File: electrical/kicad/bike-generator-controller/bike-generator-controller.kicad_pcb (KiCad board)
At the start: 2 copper layers, 100 x 115 mm, 60 parts, among them J1 DC_GEN_IN / DNP (DC VARIANT), J2 PHOENIX 1711725 / BUCK_IN, J3 J_DISPLAY_I2C, J5 J_EXT_GPIO, J6 LiPo 1S / JST-PH 2.0 / PROV., J7 J_CC_CTRL, J8 3PH_GEN_IN (1=U 2=V 3=W), J9 J_CV_CTRL, U1 INA228, U2 DFR0868 Beetle ESP32-C3, U3 MCP42100-I/SL, U4 LM5164DDAT

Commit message: wip: capture live PCB state before routing fixes
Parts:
- moved J8 8.42 mm to (61.5, 103.0)
- moved D2 7.93 mm to (71.9, 97.2)
- moved D1 3.42 mm to (84.2, 117.1)
- moved F1 3.11 mm to (79.5, 125.3)
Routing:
- net /INA228_SENSE/VBUS_SENSE: track 18.2 -> 50.1 mm
- net /POWER_PATH/RECTIFIED_RAW: track 0.00 -> 26.3 mm
- net Net-(D1-K): track 0.00 -> 11.5 mm
- net GND: track 34.9 -> 29.7 mm
- net /POWER_PATH/GEN_PHASE_V: track 12.7 -> 10.7 mm
- net /POWER_PATH/GEN_PHASE_W: track 13.7 -> 11.7 mm
- net /POWER_PATH/GEN_PHASE_U: track 12.5 -> 11.1 mm
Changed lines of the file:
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@@
 	(footprint "BikeGenerator:Fuse_Littelfuse_456_10.08x3.05mm_P9.35mm"
 		(layer "F.Cu")
-		(at 79.7375 128.4)
+		(at 79.525 125.3)
 		(descr "Littelfuse 456 Series High Current NANO2 fuse, 20A/25A/30A package. Exact recommended pad layout: pads 3.25 x 3.43 mm, 6.10 mm inner gap, 12.60 mm overall span, 9.35 mm center pitch. Body 10.08 x 3.05 mm. Pad numbering is arbitrary because the fuse is non-polarized: pad 1 left and pad 2 right in top/component view. Datasheet: https://www.littelfuse.com/assetdocs/littelfuse_fuse_456_datasheet.pdf?assetguid=d86b18f9-14fa-4764-87ff-8aec12e9a89d")
 		(property "Reference" "F1"
@@
 	(footprint "BikeGenerator:Diode_Bridge_Diotec_DBI-A_5Pin_P7.50mm"
 		(layer "F.Cu")
-		(at 73.8 104.9 -90)
+		(at 71.9 97.2 -90)
 		(descr "Diotec DBI25-xxA three-phase bridge rectifier, DBI-A vertical THT, five solder pins at 7.5 mm pitch; marking-side order left to right: - ~ ~ ~ +")
 		(property "Reference" "D2"
@@
 	(footprint "TerminalBlock_Phoenix:TerminalBlock_Phoenix_MKDS-3-3-5.08_1x03_P5.08mm_Horizontal"
 		(layer "F.Cu")
-		(at 61.7 111.4 90)
+		(at 61.4675 102.985 90)
 		(descr "Terminal Block Phoenix MKDS-3-3-5.08, 3 pins, pitch 5.08mm, size 15.2x11.2mm, drill diameter 1.3mm, pad diameter 2.6mm, http://www.farnell.com/datasheets/2138224.pdf")
 		(tags "THT Terminal Block Phoenix MKDS-3-3-5.08 pitch 5.08mm size 15.2x11.2mm drill 1.3mm pad 2.6mm")
@@
 	(footprint "Diode_SMD:D_SMC"
 		(layer "F.Cu")
-		(at 84.6 120.5 90)
+		(at 84.2 117.1 90)
 		(descr "Diode SMC (DO-214AB)")
 		(tags "Diode SMC (DO-214AB)")
@@
 	)
 	(segment
+		(start 84.2 113.7)
+		(end 83 112.5)
+		(width 2)
+		(layer "F.Cu")
+		(net "GND")
+	)
+	(segment
 		(start 91.7 87.9625)
 		(end 91.7 89.3)
@@
 	)
 	(segment
-		(start 83.5 116)
-		(end 83.5 114.5)
-		(width 2)
-		(layer "F.Cu")
-		(net "GND")
-	)
-	(segment
 		(start 91.075 114)
 		(end 91.075 111.5)
@@
 	)
 	(segment
+		(start 84.2 113.7)
+		(end 84.8 113.7)
+		(width 2)
+		(layer "F.Cu")
+		(net "GND")
+	)
+	(segment
 		(start 91.5 109.150001)
 		(end 91.5 111.4625)
@@
 	)
 	(segment
-		(start 84.6 116.4)
-		(end 86.5 114.5)
-		(width 2)
-		(layer "F.Cu")
-		(net "GND")
-	)
-	(segment
 		(start 97.625 51.4)
 		(end 99.4 51.4)
@@
 	)
 	(segment
-		(start 84.6 117.1)
-		(end 84.6 116.4)
-		(width 2)
+		(start 91.5 111.4625)
+		(end 91.4625 111.5)
+		(width 0.25)
 		(layer "F.Cu")
 		(net "GND")
 	)
 	(segment
-		(start 91.5 111.4625)
-		(end 91.4625 111.5)
-		(width 0.25)
+		(start 84.8 113.7)
+		(end 86 112.5)
+		(width 2)
 		(layer "F.Cu")
 		(net "GND")
@@
 	)
 	(segment
-		(start 84.6 117.1)
-		(end 83.5 116)
-		(width 2)
-		(layer "F.Cu")
-		(net "GND")
-	)
-	(segment
 		(start 95.2 97.5)
 		(end 94 97.5)
@@
 	)
 	(via
-		(at 86.5 114.5)
+		(at 86 112.5)
 		(size 1.2)
 		(drill 0.6)
@@
 	)
 	(via
-		(at 83.5 114.5)
+		(at 83 112.5)
 		(size 1.2)
 		(drill 0.6)
@@
 	)
 	(segment
-		(start 114.167501 129.045)
-		(end 112.212501 131)
-		(width 5)
-		(layer "B.Cu")
-		(net "GND")
-	)
-	(segment
 		(start 94.86 27.4)
 		(end 95.11 27.15)
@@
 	)
 	(segment
+		(start 113.567501 119.465)
+		(end 104.77781 119.465)
+		(width 5)
+		(layer "F.Cu")
+		(net "/INA228_SENSE/VBUS_SENSE")
+	)
+	(segment
 		(start 92 111)
 		(end 92.225 111.225)
@@
 	)
 	(segment
+		(start 99.89281 124.35)
+		(end 98.525 124.35)
+		(width 5)
+		(layer "F.Cu")
+		(net "/INA228_SENSE/VBUS_SENSE")
+	)
+	(segment
 		(start 92.225 111.225)
 		(end 92.225 117.725)
@@
 	)
 	(segment
+		(start 113.567501 119.465)
+		(end 113.567501 112.022501)
+		(width 5)
+		(layer "F.Cu")
+		(net "/INA228_SENSE/VBUS_SENSE")
+	)
+	(segment
+		(start 104.77781 119.465)
+		(end 99.89281 124.35)
+		(width 5)
+		(layer "F.Cu")
+		(net "/INA228_SENSE/VBUS_SENSE")
+	)
+	(segment
 		(start 94.375 120.2)
 		(end 98.525 124.35)
@@
 	)
 	(segment
+		(start 113.567501 112.022501)
+		(end 108.3 106.755)
+		(width 5)
+		(layer "F.Cu")
+		(net "/INA228_SENSE/VBUS_SENSE")
+	)
+	(segment
 		(start 93 118.5)
 		(end 93 118.375)
@@
 	)
 	(segment
-		(start 72.8 111.4)
-		(end 73.8 112.4)
+		(start 90.475 124.35)
+		(end 85.15 124.35)
+		(width 5)
+		(layer "F.Cu")
+		(net "Net-(D1-K)")
+	)
+	(segment
+		(start 85.15 124.35)
+		(end 84.2 125.3)
+		(width 0.25)
+		(layer "F.Cu")
+		(net "Net-(D1-K)")
+	)
+	(segment
+		(start 84.2 125.3)
+		(end 84.2 120.5)
+		(width 5)
+		(layer "F.Cu")
+		(net "Net-(D1-K)")
+	)
+	(segment
+		(start 70.185 102.985)
+		(end 71.9 104.7)
 		(width 4)
 		(layer "F.Cu")
@@
 	)
 	(segment
-		(start 61.7 111.4)
-		(end 72.8 111.4)
+		(start 61.4675 102.985)
+		(end 70.185 102.985)
 		(width 4)
 		(layer "F.Cu")
@@
 	)
 	(segment
-		(start 72.38 106.32)
-		(end 73.8 104.9)
+		(start 61.4675 97.905)
+		(end 71.195 97.905)
 		(width 4)
 		(layer "F.Cu")
@@
 	)
 	(segment
-		(start 61.7 106.32)
-		(end 72.38 106.32)
+		(start 71.195 97.905)
+		(end 71.9 97.2)
 		(width 4)
 		(layer "F.Cu")
@@
 	)
 	(segment
-		(start 69.96 101.24)
-		(end 73.8 97.4)
+		(start 71.9 112.2)
+		(end 71.9 122.35)
+		(width 5)
+		(layer "F.Cu")
+		(net "/POWER_PATH/RECTIFIED_RAW")
+	)
+	(segment
+		(start 68.765 119.215)
+		(end 74.85 125.3)
+		(width 5)
+		(layer "F.Cu")
+		(net "/POWER_PATH/RECTIFIED_RAW")
+	)
+	(segment
+		(start 61.2325 119.215)
+		(end 68.765 119.215)
+		(width 5)
+		(layer "F.Cu")
+		(net "/POWER_PATH/RECTIFIED_RAW")
+	)
+	(segment
+		(start 61.4675 92.825)
+		(end 64.5925 89.7)
 		(width 4)
 		(layer "F.Cu")
@@
 	)
 	(segment
-		(start 61.7 101.24)
-		(end 69.96 101.24)
+		(start 64.5925 89.7)
+		(end 71.9 89.7)
 		(width 4)
 		(layer "F.Cu")

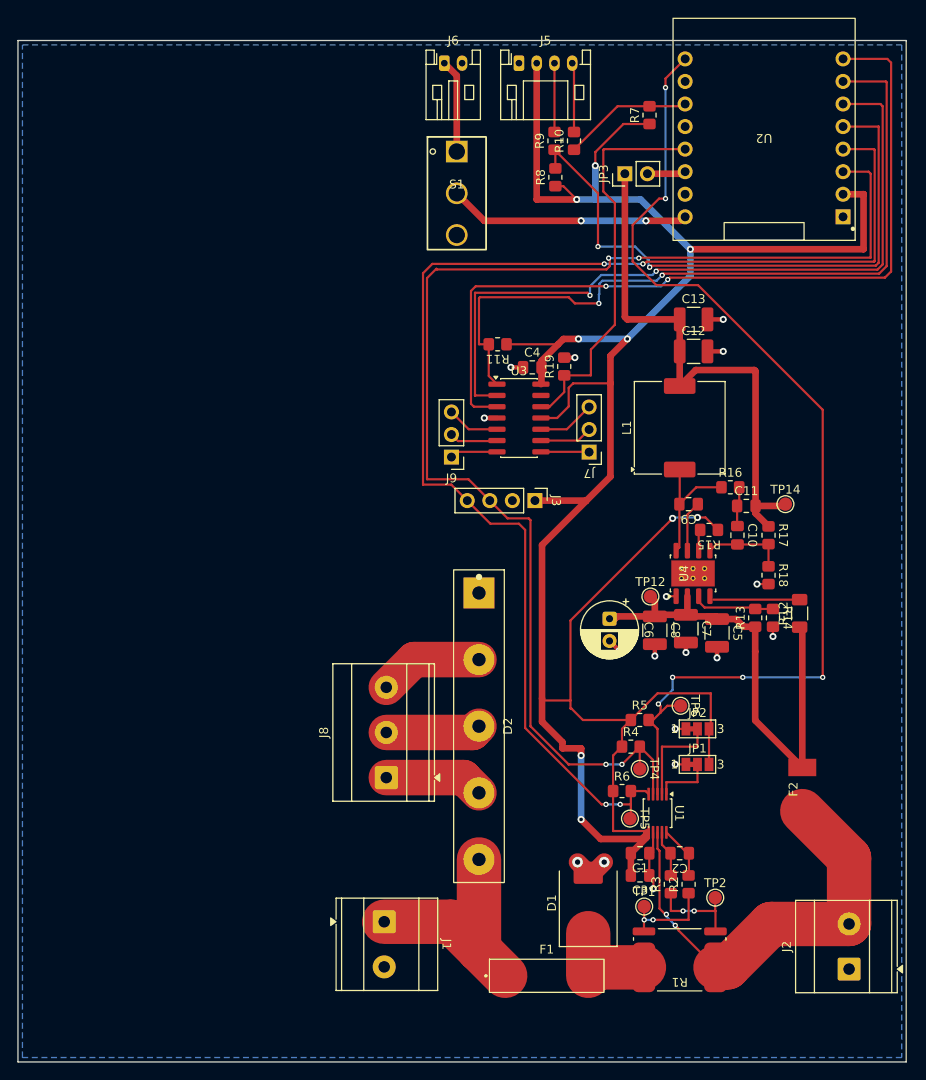
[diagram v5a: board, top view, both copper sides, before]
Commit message: feat: close controller v1 design and define integrated v2
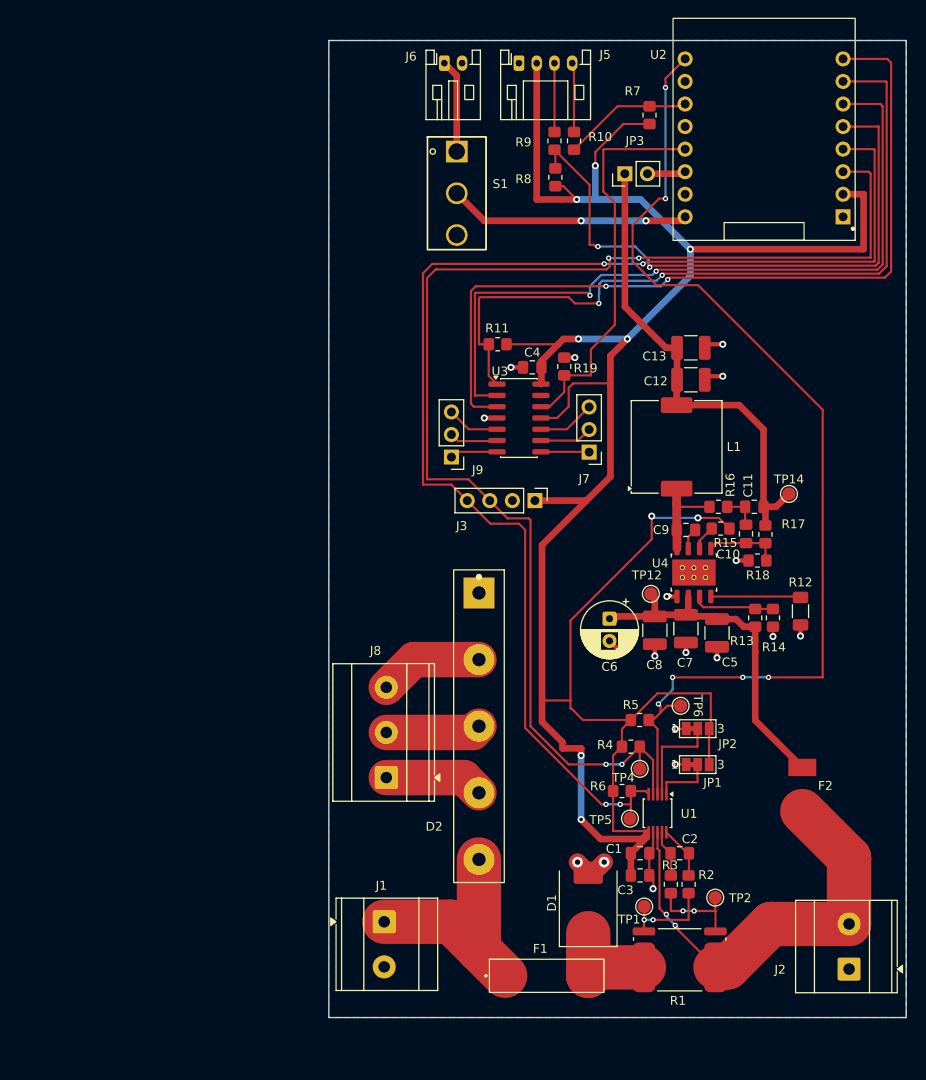
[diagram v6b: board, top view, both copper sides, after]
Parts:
- F2: value F_AUX / PROVISOIRE -> 0449001.MR / 1A 125V Slo-Blo
- J1: value DC_GEN_IN / DNP (DC VARIANT) -> DC_GEN_IN / DIRECT DC VARIANT
- TP12: value ~ -> AUX_IN_PROTECTED
- U1: value INA228 -> INA228AIDGSR
- moved C12 3.21 mm to (95.8, 58.2)
- moved C13 3.21 mm to (95.8, 54.6)
- moved C9 2.92 mm to (95.2, 75.1)
- moved R16 2.58 mm to (98.8, 72.5)
- moved L1 2.18 mm to (94.2, 65.8)
- moved R18 2.07 mm to (103.2, 78.5), turned to 180 degrees
- moved R15 1.31 mm to (99.1, 75.0)
- moved TP14 1.22 mm to (106.8, 71.0)
- moved C10 0.97 mm to (102.0, 75.5)
- moved C11 0.91 mm to (102.9, 72.5)
- moved R17 0.36 mm to (104.2, 75.6)
- moved TP12 0.30 mm to (91.2, 82.3)
- moved R12 0.27 mm to (108.1, 84.2)
- moved U4 0.14 mm to (96.1, 79.9)
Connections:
- R12 pad 1: /AUX_SUPPLY/AUX_IN_PROTECTED -> GND
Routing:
- net /AUX_SUPPLY/AUX_IN_PROTECTED: track 56.6 -> 40.8 mm
- net /AUX_SUPPLY/AUX_5V: track 61.0 -> 55.7 mm
- net /AUX_SUPPLY/SW: track 14.8 -> 10.5 mm
- net /AUX_SUPPLY/BST: track 5.72 -> 2.42 mm
- net +3V3: track 280.8 -> 283.7 mm
- net GND: track 29.7 -> 31.9 mm, vias 17 -> 18
- net /AUX_SUPPLY/AUX_PGOOD: track 2.41 -> 3.68 mm
- net /AUX_SUPPLY/FB: track 9.40 -> 8.40 mm
- net /AUX_SUPPLY/UVLO: track 9.32 -> 9.91 mm
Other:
- board size 100 x 115 mm -> 65 x 110 mm

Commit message: feat(pcb): finalize V1 controller layout
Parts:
- removed S1: 1101M2S3CQE2 / BAT ON-OFF, BikeGenerator:SW_1101M2S3CQE2
- added H1: MountingHole_3.2mm_M3_BoardOnly, BikeGenerator:MountingHole_3.2mm_M3_BoardOnly, F.Cu at (55.0, 25.0)
- added H2: MountingHole_3.2mm_M3_BoardOnly, BikeGenerator:MountingHole_3.2mm_M3_BoardOnly, F.Cu at (54.5, 112.0)
- added H3: MountingHole_3.2mm_M3_BoardOnly, BikeGenerator:MountingHole_3.2mm_M3_BoardOnly, F.Cu at (115.0, 55.0)
- added H4: MountingHole_3.2mm_M3_BoardOnly, BikeGenerator:MountingHole_3.2mm_M3_BoardOnly, F.Cu at (116.0, 104.5)
- added JP4: BATTERY CONNECT / DISCONNECT, Connector_PinHeader_2.54mm:PinHeader_1x02_P2.54mm_Vertical, F.Cu at (73.5, 34.0)
- J5: footprint Connector_JST:JST_PH_S4B-PH-K_1x04_P2.00mm_Horizontal -> Connector_PinHeader_2.54mm:PinHeader_1x04_P2.54mm_Vertical
- R1: footprint Resistor_SMD:R_Shunt_Isabellenhuette_BVR4026 -> BikeGenerator:R_Shunt_Isabellenhuette_BVR4026
- moved J8 41.7 mm to (59.0, 61.3), turned to -90 degrees
- moved R10 10.4 mm to (89.5, 23.5), turned to 180 degrees
- moved J5 9.42 mm to (85.5, 25.0), turned to -90 degrees
- moved J6 6.30 mm to (73.5, 25.7), turned to -90 degrees
- moved J1 2.83 mm to (59.0, 121.0)
- moved D2 1.91 mm to (70.0, 97.0), turned to 90 degrees
- moved D1 1.70 mm to (82.5, 117.1)
- moved C10 0.79 mm to (102.8, 75.6)
- moved R18 0.79 mm to (104.0, 78.6)
- moved R17 0.79 mm to (104.9, 75.6)
- moved C11 0.79 mm to (103.7, 72.5)
- moved R15 0.35 mm to (99.5, 75.0)
- moved R9 0.32 mm to (80.5, 31.0)
- moved C9 0.28 mm to (95.0, 74.9)
- moved R16 0.21 mm to (98.8, 72.3)
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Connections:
- J8 pad 1: /POWER_PATH/GEN_PHASE_U -> /POWER_PATH/GEN_PHASE_W
- J8 pad 2: /POWER_PATH/GEN_PHASE_V -> /POWER_PATH/GEN_PHASE_U
- J8 pad 3: /POWER_PATH/GEN_PHASE_W -> /POWER_PATH/GEN_PHASE_V
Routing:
- net /POWER_PATH/GEN_PHASE_W: track 11.7 -> 62.7 mm
- net +3V3: track 283.7 -> 238.3 mm, vias 9 -> 7
- net /POWER_PATH/RECTIFIED_RAW: track 26.3 -> 62.2 mm
- net /POWER_PATH/GEN_PHASE_V: track 10.7 -> 35.2 mm
- net /POWER_PATH/GEN_PHASE_U: track 11.1 -> 31.8 mm
- net /CONNECTORS/GPIO8_ACTION: track 14.6 -> 8.26 mm
- net Net-(J5-Pin_4): track 7.83 -> 12.8 mm
- net /MCU/BAT_CTRL: track 27.2 -> 24.0 mm
- net GND: track 31.9 -> 35.1 mm
- net Net-(J5-Pin_3): track 7.75 -> 5.03 mm
- net /I2C_SCL: track 148.7 -> 150.9 mm
- net /I2C_SDA: track 147.1 -> 149.1 mm
- net /AUX_SUPPLY/RIPPLE: track 4.07 -> 5.29 mm
- net /AUX_SUPPLY/SW: track 10.5 -> 11.5 mm
- net /AUX_SUPPLY/FB: track 8.40 -> 9.20 mm
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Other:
- board size 65 x 110 mm -> 70 x 110 mm
- board text added: "R10"

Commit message: feat(controller): finalize V1 design and sourcing
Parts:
- J8: value 3PH_GEN_IN (1=U 2=V 3=W) -> 3PH_GEN_IN (1=W 2=U 3=V)
- U1: value INA228AIDGSR -> INA238AIDGSR
- moved H2 5.07 mm to (59.5, 111.6)
- moved J2 2.36 mm to (111.6, 125.8)
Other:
- board text added: "+"
- board text added: "-"
